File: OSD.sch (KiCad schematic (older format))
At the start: 16 parts, among them U6 MAX7456EUI+, Y1 27MHz

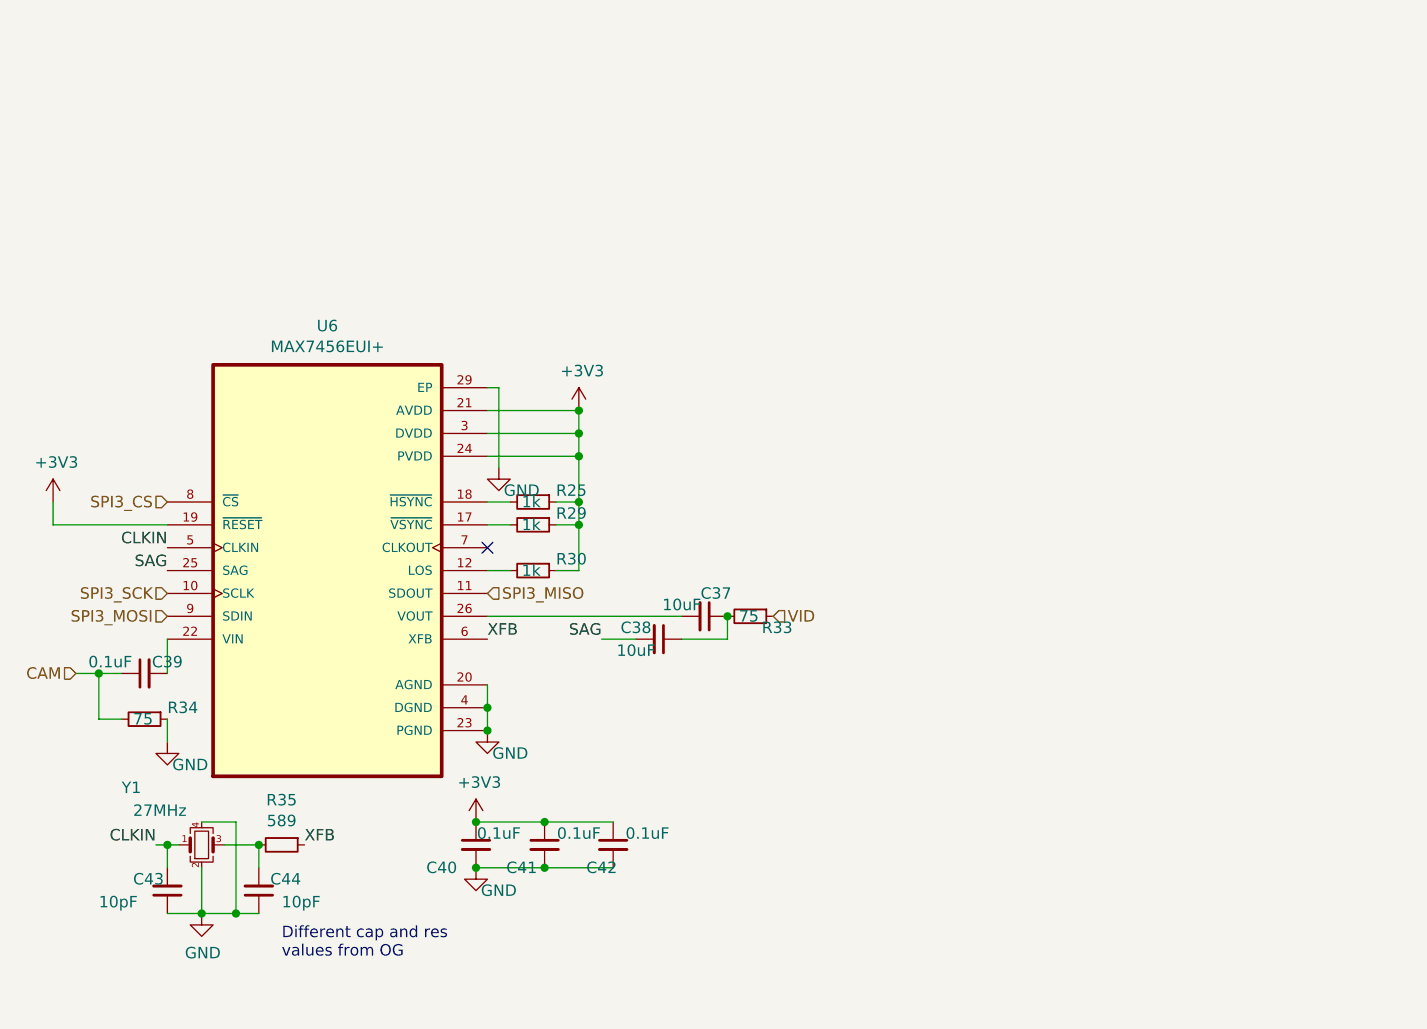
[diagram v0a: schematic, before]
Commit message: Updated the schematics to include pictures
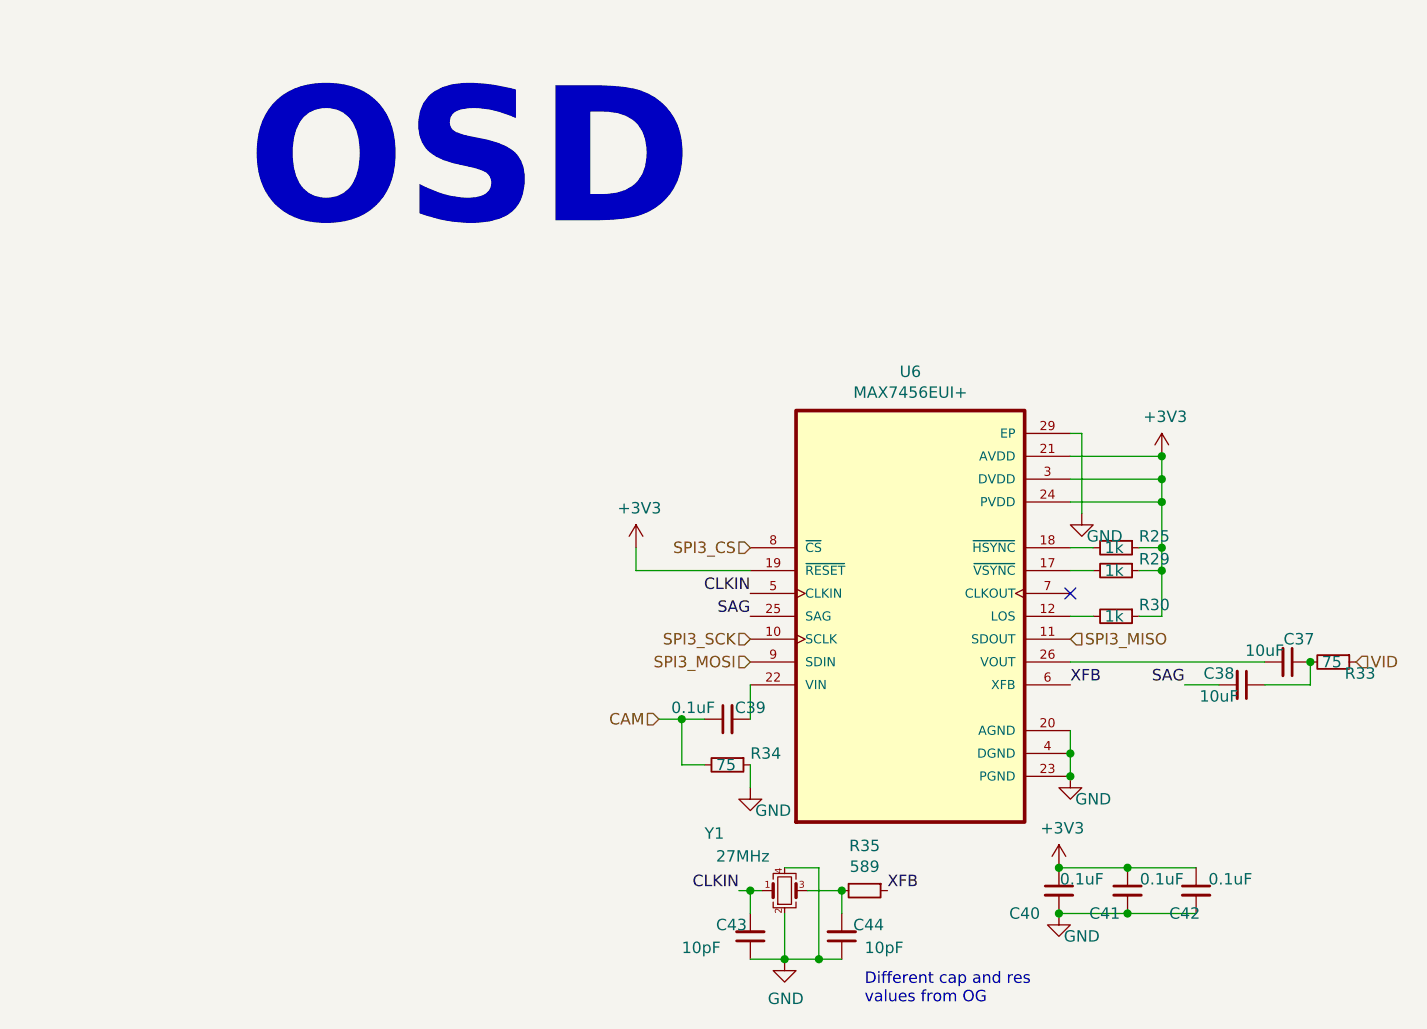
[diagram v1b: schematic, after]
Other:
- note added: "OSD"
- moved on the sheet: C37, C38, C39, C40, C41, C42, C43, C44, R25, R29, R30, R33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
